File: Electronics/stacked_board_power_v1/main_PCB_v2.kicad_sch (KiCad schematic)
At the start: 74 parts, among them J101 Conn_01x02, J102 Conn_01x02, J104 Conn_01x02, J105 Conn_01x02, J106 Conn_01x02, J108 Conn_01x02, J109 Conn_02x20_Odd_Even, K101 G2RL-1-E, U101 TVS2700DRV, U102 TPS16416DRCR, U103 LMR43620MB5RPER, U104 LMR43620MB5RPER, U105 LMR43620MB5RPER, U106 TPS25961DRVR, U107 TPS25961DRVR

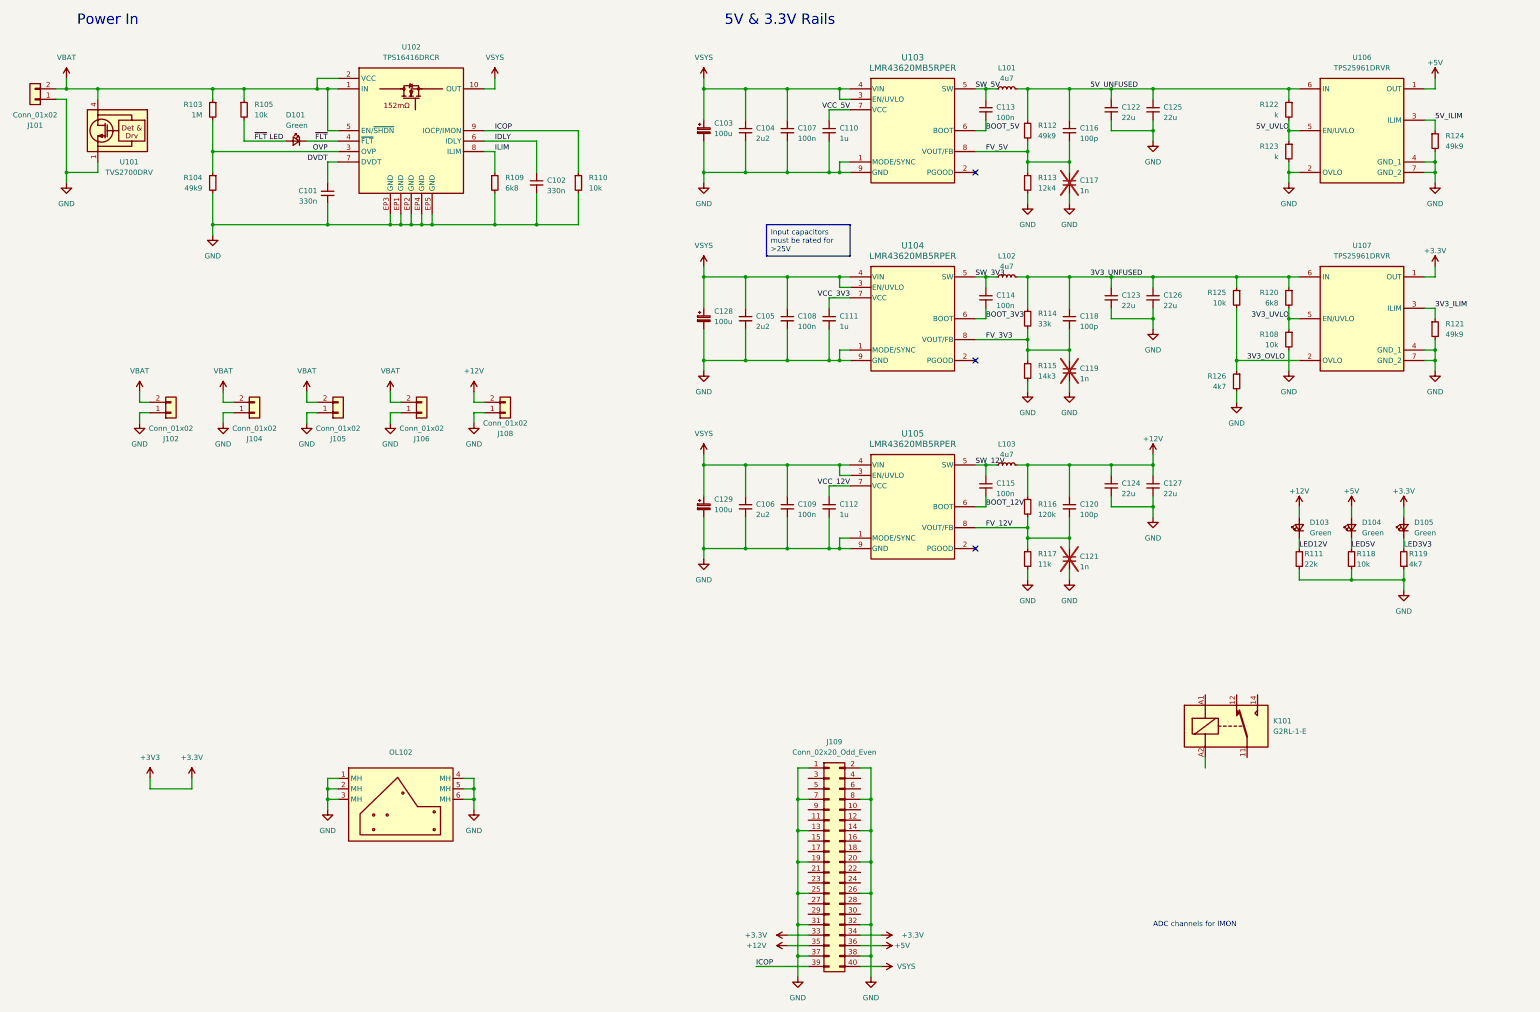
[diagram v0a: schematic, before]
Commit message: power pcb schematic done
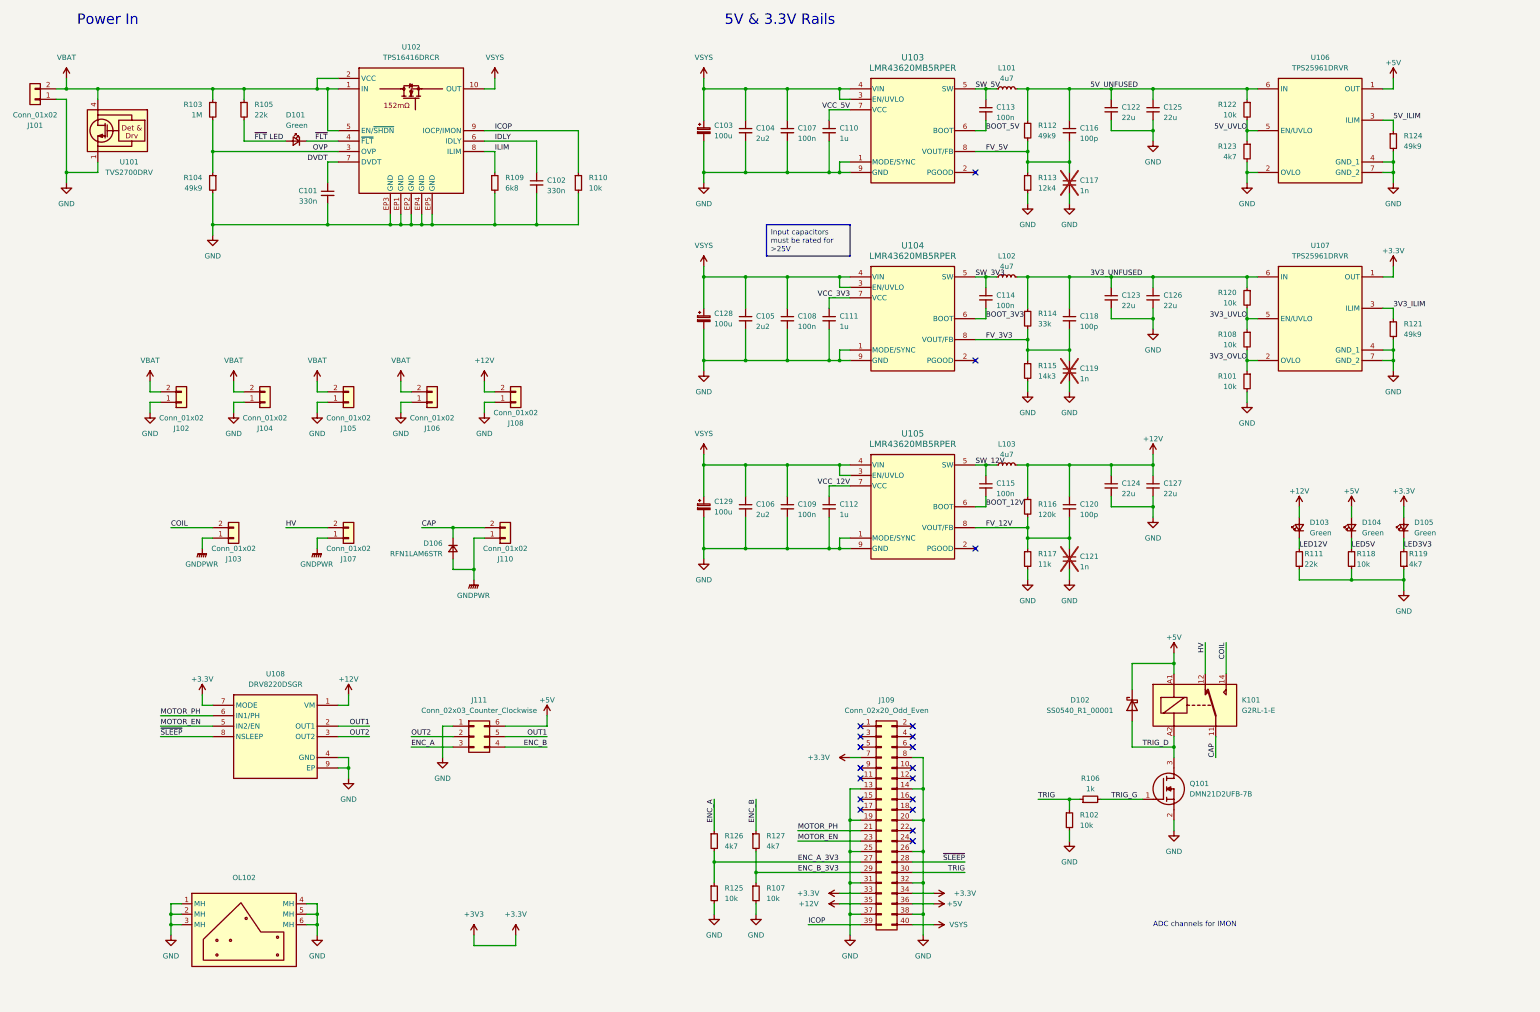
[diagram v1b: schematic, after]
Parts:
- added D102: SS0540_R1_00001, Diode_SMD:D_SOD-123, symbol Device:D_Schottky
- added D106: RFN1LAM6STR, symbol Device:D_Small
- added J103, J107, J110: Conn_01x02, Connector_AMASS:AMASS_XT30U-F_1x02_P5.0mm_Vertical, symbol Connector_Generic:Conn_01x02
- added J111: Conn_02x03_Counter_Clockwise, Connector_IDC:IDC-Header_2x03_P2.54mm_Vertical, symbol Connector_Generic:Conn_02x03_Counter_Clockwise
- added Q101: DMN21D2UFB-7B, watch_footprints:DMN21D2UFB7B, symbol DMN21D2UFB-7B:DMN21D2UFB-7B
- added R101, R102, R107: 10k, Resistor_SMD:R_0402_1005Metric, symbol Device:R_Small
- added R106: 1k, Resistor_SMD:R_0402_1005Metric, symbol Device:R_Small
- added R127: 4k7, Resistor_SMD:R_0402_1005Metric, symbol Device:R_Small
- added U108: DRV8220DSGR, SSL Footprints:SON50P200X200X80-9N, symbol DRV8220DSGR:DRV8220DSGR
- R105: value 10k -> 22k
- R120: value 6k8 -> 10k
- R122: value k -> 10k
- R123: value k -> 4k7
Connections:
- net +12V: now also U108.1 (VM)
- net +3.3V: now also J109.7 (Pin_7), U108.7 (MODE)
- net +5V: now also K101.A1, D102.1 (K), J111.6 (Pin_6)
- net 3V3_OVLO: now also R108.2, R101.1; no longer R125.2, R126.1
- net 3V3_UNFUSED: no longer R125.1
- net GND: now also R125.2, J111.1 (Pin_1), Q101.2 (S), R101.2, R102.2, R107.2, U108.4 (GND), U108.9 (EP); no longer J109.1 (Pin_1), J109.2 (Pin_2), J109.7 (Pin_7), R108.2, R126.2
- net CAP: now reaches K101.11
- net CAP: now also D106.1 (K), J110.2 (Pin_2)
- net HV: now reaches K101.12
- net HV: now also J107.2 (Pin_2)
- net COIL: now reaches K101.14
- net COIL: now also J103.2 (Pin_2)
- net TRIG_D: now reaches K101.A2
- net TRIG_D: now also D102.2 (A), Q101.3 (D)
- net MOTOR_PH: now reaches J109.21 (Pin_21)
- net MOTOR_PH: now also U108.6 (IN1/PH)
- net MOTOR_EN: now reaches J109.23 (Pin_23)
- net MOTOR_EN: now also U108.5 (IN2/EN)
- net ENC_A_3V3: now reaches J109.27 (Pin_27)
- net ENC_A_3V3: now also R125.1, R126.2
- net ~{SLEEP}: now reaches J109.28 (Pin_28)
- net ~{SLEEP}: now also U108.8 (NSLEEP)
- net ENC_B_3V3: now reaches J109.29 (Pin_29)
- net ENC_B_3V3: now also R107.1, R127.2
- net TRIG: now reaches J109.30 (Pin_30)
- net TRIG: now also R102.1, R106.1
- new net ENC_A: J111.3 (Pin_3), R126.1
- new net ENC_B: J111.4 (Pin_4), R127.1
- new net GNDPWR: D106.2 (A), J103.1 (Pin_1), J107.1 (Pin_1), J110.1 (Pin_1)
- new net OUT1: J111.5 (Pin_5), U108.2 (OUT1)
- new net OUT2: J111.2 (Pin_2), U108.3 (OUT2)
- new net TRIG_G: Q101.1 (G), R106.2
- no-connect marks 3 -> 19
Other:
- moved on the sheet: J102, J104, J105, J106, J108, J109, K101, OL102, R108, R120, R121, R122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

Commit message: Power board done
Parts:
- removed R101, R108, R120, R122: 10k, Resistor_SMD:R_0402_1005Metric, symbol Device:R_Small
- removed R121, R124: 49k9, Resistor_SMD:R_0402_1005Metric, symbol Device:R_Small
- removed R123: 4k7, Resistor_SMD:R_0402_1005Metric, symbol Device:R_Small
- removed U106, U107: TPS25961DRVR, SON65P200X200X80-7N, symbol TPS25961DRVR:TPS25961DRVR
- added C130, C131, C134: 100n, Capacitor_SMD:C_0402_1005Metric, symbol Device:C_Small
- added C132, C133: 330n, Capacitor_SMD:C_0402_1005Metric, symbol Device:C_Small
- added R129, R130, R131, R132, R133, R134, R136, R138: 10k, Resistor_SMD:R_0402_1005Metric, symbol Device:R_Small
- added R135: 6k8, Resistor_SMD:R_0402_1005Metric, symbol Device:R_Small
- added R137: 3k3, Resistor_SMD:R_0402_1005Metric, symbol Device:R_Small
- added U109, U110: TPS16416DRCR, TPS74901DRCR, symbol TPS16416DRCR:TPS16416DRCR
- C101, C102: footprint Capacitor_SMD:C_0603_1608Metric -> Capacitor_SMD:C_0402_1005Metric
- D106: footprint (none) -> Diode_SMD:D_SOD-128
- OL102: footprint (none) -> SSL Footprints:main_board_outline_v3
- Q101: footprint watch_footprints:DMN21D2UFB7B -> SSL Footprints:DMN21D2UFB7B
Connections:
- net +12V: now also C130.1
- net +3.3V: now also U110.10 (OUT)
- net +5V: now also U109.10 (OUT)
- net 3V3_UNFUSED: now also R129.1, R134.1, U110.1 (IN), U110.2 (VCC)
- net 5V_UNFUSED: now also R136.1, R138.1, U109.1 (IN), U109.2 (VCC)
- net GND: now also C130.2, C131.2, C132.2, C133.2, C134.2, R130.2, R131.2, R132.2, R133.2, R135.2, R137.2, U109.EP1 (GND), U109.EP2 (GND), U109.EP3 (GND), U109.EP4 (GND), U109.EP5 (GND), U110.EP1 (GND), U110.EP2 (GND), U110.EP3 (GND), U110.EP4 (GND), U110.EP5 (GND)
- net OUT1: now also J111.2 (Pin_2); no longer J111.5 (Pin_5)
- net OUT2: now also J111.5 (Pin_5); no longer J111.2 (Pin_2)
- net PGOOD_3V3: now reaches U104.2 (PGOOD)
- net PGOOD_3V3: now also R129.2, U110.5 (EN/~{SHDN})
- net PGOOD_5V: now reaches U103.2 (PGOOD)
- net PGOOD_5V: now also R138.2, U109.5 (EN/~{SHDN})
- new net DVDT_3V3: C131.1, U110.7 (DVDT)
- new net DVDT_5V: C134.1, U109.7 (DVDT)
- new net ICOP_3V3: R130.1, U110.9 (IOCP/IMON)
- new net ICOP_5V: R133.1, U109.9 (IOCP/IMON)
- new net IDLY_3V3: C132.1, U110.6 (IDLY)
- new net IDLY_5V: C133.1, U109.6 (IDLY)
- new net ILIM_3V3: R131.1, U110.8 (ILIM)
- new net ILIM_5V: R132.1, U109.8 (ILIM)
- new net OVP_3V3: R134.2, R135.1, U110.3 (OVP)
- new net OVP_5V: R136.2, R137.1, U109.3 (OVP)
- no-connect marks 19 -> 20
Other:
- moved on the sheet: C116, C118, C120, R112, R114, R116, U108
